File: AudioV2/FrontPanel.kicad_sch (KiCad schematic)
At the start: 32 parts, among them SW402 Cosland 2MS1 PWR, SW501 Cosland 2MD1 DEST, U1609 XC8107AC20MR-G, U1610 MCP23017 (UI 0x22)

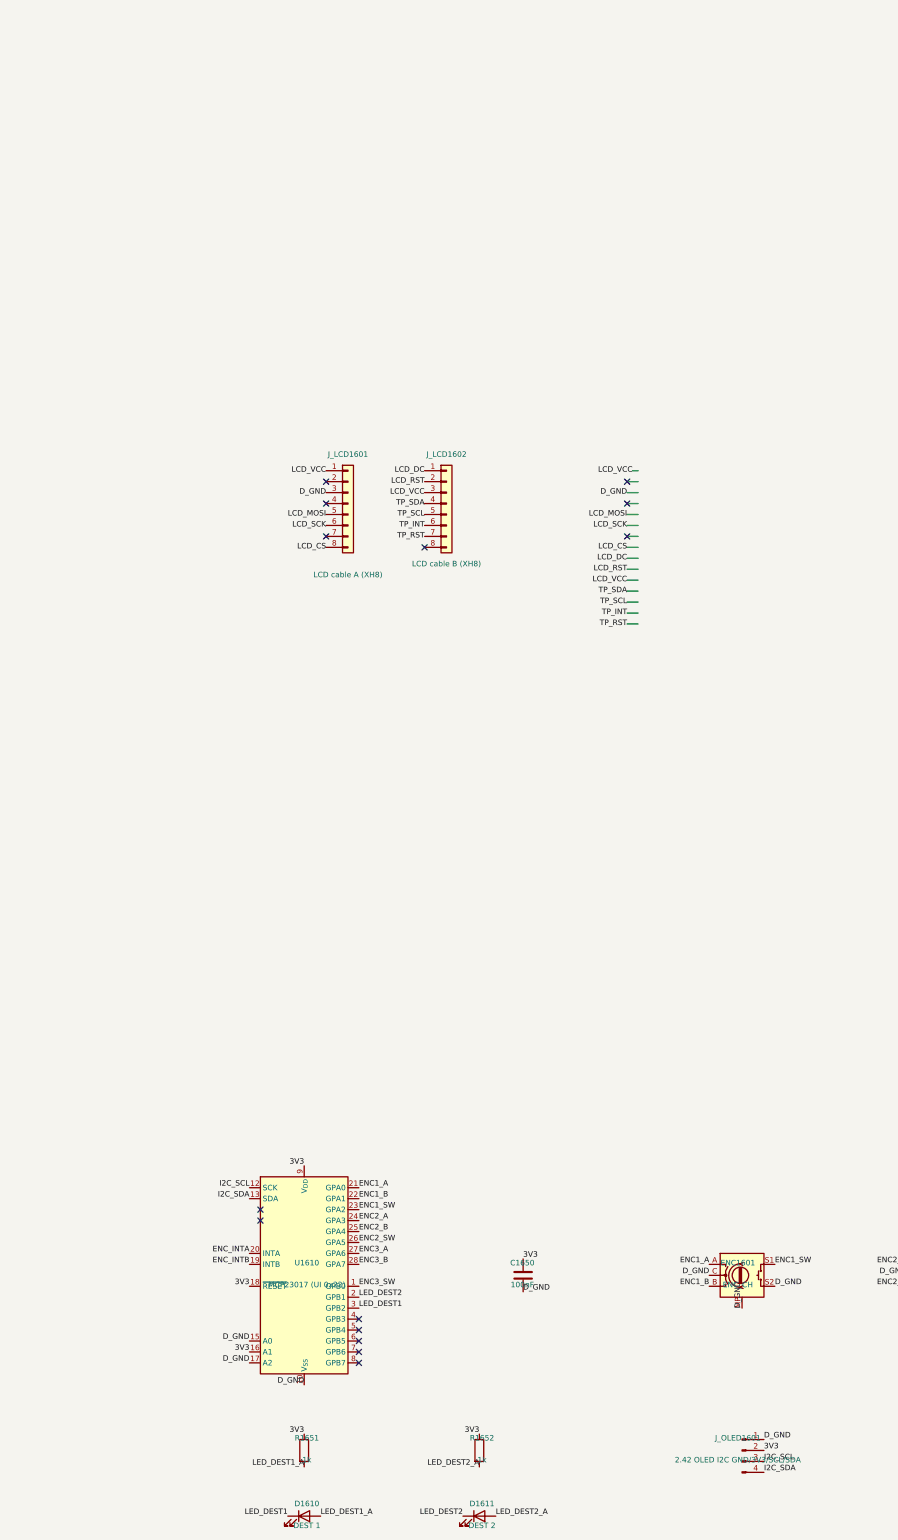
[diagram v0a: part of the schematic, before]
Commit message: AudioV2: OLED を外し、状態表示を LCD 寄せ（Switch/Relay 共通 FP）
操作系（ENC/DEST/ポット）はそのまま。FrontPanel から J_OLED を削除し、
AmpBankSwitch / AmpBankRelay 共通の表示経路を Waveshare LCD に寄せる。

Co-authored-by: m_arino <indare@users.noreply.github.com>
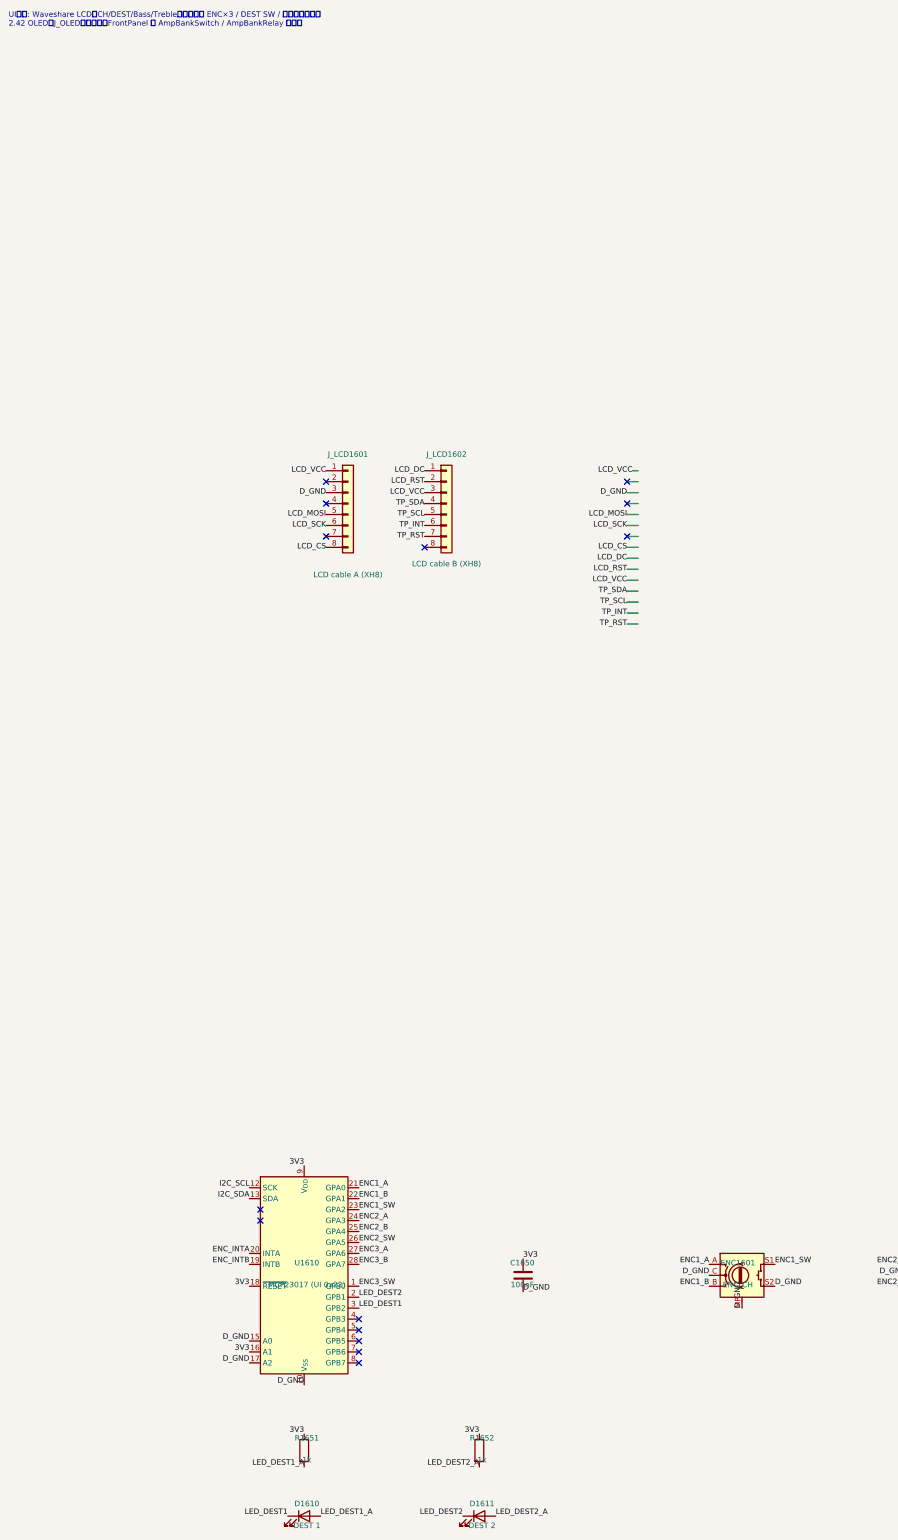
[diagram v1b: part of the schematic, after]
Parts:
- removed J_OLED1601: 2.42 OLED I2C GND/3V3/SCL/SDA, Connector_JST:JST_XH_B4B-XH-A_1x04_P2.50mm_Vertical, symbol Connector:Conn_01x04_Pin
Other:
- note added: "UI表示: Waveshare LCD（CH/DEST/Bass/Treble）。操作は ENC×3 / DEST SW / ポットのまま。 2.42 OLED（J_OLED）は廃止。FrontPanel は AmpBankSwitch / AmpBankRelay 共通。"
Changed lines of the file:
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@@
 		)
 	)
-	(label "I2C_SDA"
-		(at 226.06 386.08 0)
-		(effects
-			(font
-				(size 1.27 1.27)
-			)
-			(justify left bottom)
-		)
-	)
 	(label "LED_DEST2_A"
 		(at 163.83 396.24 0)
@@
 		)
 	)
-	(label "D_GND"
-		(at 226.06 378.46 0)
-		(effects
-			(font
-				(size 1.27 1.27)
-			)
-			(justify left bottom)
-		)
-	)
 	(label "A_GND"
 		(at 436.88 342.9 180)
@@
 		)
 	)
-	(label "3V3"
-		(at 226.06 381 0)
-		(effects
-			(font
-				(size 1.27 1.27)
-			)
-			(justify left bottom)
-		)
-	)
 	(label "LCD_VCC"
 		(at 124.46 153.67 180)
@@
 		)
 	)
-	(label "I2C_SCL"
-		(at 226.06 383.54 0)
-		(effects
-			(font
-				(size 1.27 1.27)
-			)
-			(justify left bottom)
-		)
-	)
 	(label "ENC3_SW"
 		(at 132.08 342.9 0)
@@
 	)
 	(symbol
-		(lib_id "Connector:Conn_01x04_Pin")
-		(at 220.98 381 0)
-		(unit 1)
-		(body_style 1)
-		(exclude_from_sim no)
-		(in_bom yes)
-		(on_board yes)
-		(in_pos_files yes)
-		(dnp no)
-		(fields_autoplaced yes)
-		(property "Reference" "J_OLED1601"
-			(at 220 378.1 0)
-			(show_name no)
-			(do_not_autoplace no)
-			(effects
-				(font
-					(size 1.27 1.27)
-				)
-			)
-		)
-		(property "Value" "2.42 OLED I2C GND/3V3/SCL/SDA"
-			(at 220 383.18 0)
-			(show_name no)
-			(do_not_autoplace no)
-			(effects
-				(font
-					(size 1.27 1.27)
-				)
-			)
-		)
-		(property "Footprint" "Connector_JST:JST_XH_B4B-XH-A_1x04_P2.50mm_Vertical"
-			(at 0 0 0)
-			(hide yes)
-			(show_name no)
-			(do_not_autoplace no)
-			(effects
-				(font
-					(size 1.27 1.27)
-				)
-			)
-		)
-		(property "Datasheet" ""
-			(at 0 0 0)
-			(hide yes)
-			(show_name no)
-			(do_not_autoplace no)
-			(effects
-				(font
-					(size 1.27 1.27)
-				)
-			)
-		)
-		(property "Description" ""
-			(at 0 0 0)
-			(hide yes)
-			(show_name no)
-			(do_not_autoplace no)
-			(effects
-				(font
-					(size 1.27 1.27)
-				)
-			)
-		)
-		(pin "1"
-		)
-		(pin "2"
-		)
-		(pin "3"
-		)
-		(pin "4"
-		)
-		(instances
-			(project "AudioV2Case"
-				(path "/a1000001-0001-4001-8001-000000000001/b2000020-0020-4020-8020-000000000020"
-					(reference "J_OLED1601")
-					(unit 1)
-				)
-			)
-		)
-	)
-	(symbol
 		(lib_id "Connector_Generic:Conn_01x08")
 		(at 457.2 372.11 0)
@@
 		)
 	)
-)
+	(text "UI表示: Waveshare LCD（CH/DEST/Bass/Treble）。操作は ENC×3 / DEST SW / ポットのまま。\n2.42 OLED（J_OLED）は廃止。FrontPanel は AmpBankSwitch / AmpBankRelay 共通。"
+		(exclude_from_sim no)
+		(at 50.8 50.8 0)
+		(effects
+			(font
+				(size 1.27 1.27)
+			)
+			(justify left bottom)
+		)
+	))
